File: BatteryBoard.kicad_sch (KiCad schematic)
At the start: 19 parts, among them J1 Keystone-1042, J11 Conn_01x12_MountingPin, J14 Conn_01x04, J15 Conn_01x04, J2 Keystone-1042, J3 Keystone-1042, J4 Keystone-1042, J5 Keystone-1042, J6 Keystone-1042, SW1 SW_SPST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

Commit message: Finish v1 schematic
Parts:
- removed J15: Conn_01x04, symbol Connector_Generic:Conn_01x04
- H1, H2, H3, H4: footprint custom-footprints:MountingHole_3.2mm_M3_DIN965_PadMOD -> BatteryBoard:MountingHole
- J1, J2, J3, J4, J5, J6: footprint KEYSTONE-1042 -> BatteryBoard:Keystone_1042
- J11: value Conn_01x12_MountingPin -> 200528-0120; footprint (none) -> Connector_FFC-FPC:Molex_200528-0120_1x12-1MP_P1.00mm_Horizontal
- J14: value Conn_01x04 -> XT30PW; footprint (none) -> BatteryBoard:AMASS_XT30PW-M; symbol Connector_Generic:Conn_01x04 -> Connector_Generic_MountingPin:Conn_01x02_MountingPin
- SW1, SW2, SW3, SW4: now not fitted
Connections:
- net EN_BURN1 is gone; now on net +3V3: J11.3 (Pin_3)
- net EN_BURN2 is gone; now on net GND: J11.4 (Pin_4)
- net EN_BURN3 is gone; now on net GND: J11.5 (Pin_5)
- net +BATT: no longer J14.1 (Pin_1), J14.2 (Pin_2)
- net B-: now also J5.1 (NEG); no longer J5.2 (POS)
- net BM: now also J5.2 (POS); no longer J5.1 (NEG)
- net GND: now also J14.MP (MountPin); no longer J11.1 (Pin_1), J11.7 (Pin_7), J14.3 (Pin_3), J14.4 (Pin_4)
- net PACK+: now also J14.1 (Pin_1)
- net PACK-: now also J14.2 (Pin_2)
- net BURN_RELAY_A renamed +3V3
- net +3V3: now also J11.1 (Pin_1)
- net EN_BURN4 renamed CHRG_STAT
- net SCL renamed SCL1
- net SDA renamed SDA1
- new net DCHRG_STAT: J11.7 (Pin_7)
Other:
- removed sheet BurnWireControl
- moved on the sheet: H1, H2, H3, H4, J5

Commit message: Cleanup component designators
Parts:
- removed TP19, TP24: TestPoint, TestPoint:TestPoint_Loop_D1.80mm_Drill1.0mm_Beaded, symbol Connector:TestPoint
- added J9: 1985807, symbol Connector_Generic:Conn_01x02
- J8: renamed from J14; value XT30PW -> 1985807; footprint BatteryBoard:AMASS_XT30PW-M -> (none); symbol Connector_Generic_MountingPin:Conn_01x02_MountingPin -> Connector_Generic:Conn_01x02
- renumbered J11 to J7
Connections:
- net GND: no longer J8.MP (MountPin)
- net PACK+: now also J9.1 (Pin_1)
- net PACK-: now also J9.2 (Pin_2)
- net Fuel_Alert renamed ALRT
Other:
- note added: "FPC Ribbon cable I/O Connection to Mainboard"
- note added: "Terminal Block Power Connection to Mainboard"
- note removed: "FPC Ribbon cable I/O Connections to Mainboard"
- moved on the sheet: J7

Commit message: Complete layout
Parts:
- removed J1, J2, J3, J4: Keystone-1042, BatteryBoard:Keystone_1042, symbol BatteryBoard:Keystone-1042
- removed J8, J9: 1985807, symbol Connector_Generic:Conn_01x02
- removed SW1, SW2, SW3, SW4: SW_SPST, symbol Switch:SW_SPST
- added J1, J3: Keystone-1048, BatteryBoard:BAT_1048, symbol BatteryBoard:Keystone-1048
- added J8: 282834-4, BatteryBoard:TE_282834-4, symbol Connector_Generic:Conn_01x04
- J7: value 200528-0120 -> 200528-0100; footprint Connector_FFC-FPC:Molex_200528-0120_1x12-1MP_P1.00mm_Horizontal -> Connector_FFC-FPC:Molex_200528-0100_1x10-1MP_P1.00mm_Horizontal; symbol Connector_Generic_MountingPin:Conn_01x12_MountingPin -> Connector_Generic_MountingPin:Conn_01x10_MountingPin
- renumbered J5 to J2, J6 to J4
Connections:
- net CHRG_STAT is gone; now on net SDA1: J7.6 (Pin_6)
- net DCHRG_STAT is gone; now on net GND: J7.7 (Pin_7)
- net +3V3: now also J7.10 (Pin_10), J7.9 (Pin_9); no longer J7.1 (Pin_1), J7.2 (Pin_2), J7.3 (Pin_3)
- net ALRT: now also J7.4 (Pin_4); no longer J7.10 (Pin_10)
- net B+: now also J3.2 (POS), J3.4 (POS)
- net B-: now also J1.1 (NEG), J1.3 (NEG)
- net BM: now also J1.2 (POS), J1.4 (POS), J3.1 (NEG), J3.3 (NEG)
- net GND: now also J7.1 (Pin_1), J7.8 (Pin_8); no longer J7.11 (Pin_11), J7.12 (Pin_12), J7.4 (Pin_4), J7.5 (Pin_5)
- net PACK+: now also J8.1 (Pin_1), J8.3 (Pin_3)
- net PACK-: now also J8.2 (Pin_2), J8.4 (Pin_4)
- net SCL1: now also J7.5 (Pin_5); no longer J7.8 (Pin_8)
- net SDA1: no longer J7.9 (Pin_9)
- new net CSTAT: J7.3 (Pin_3)
- new net DSTAT: J7.2 (Pin_2)
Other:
- note removed: "INHIBIT SWITCHES"
- note removed: "Normally closed inhibit switches Disconnect PACK+ from +BATT when pressed (High-side inhibit) Disconnect PACK- from GND when pressed (Low-side inhibit)"
- moved on the sheet: H1, H2, H3, H4, J2, J4

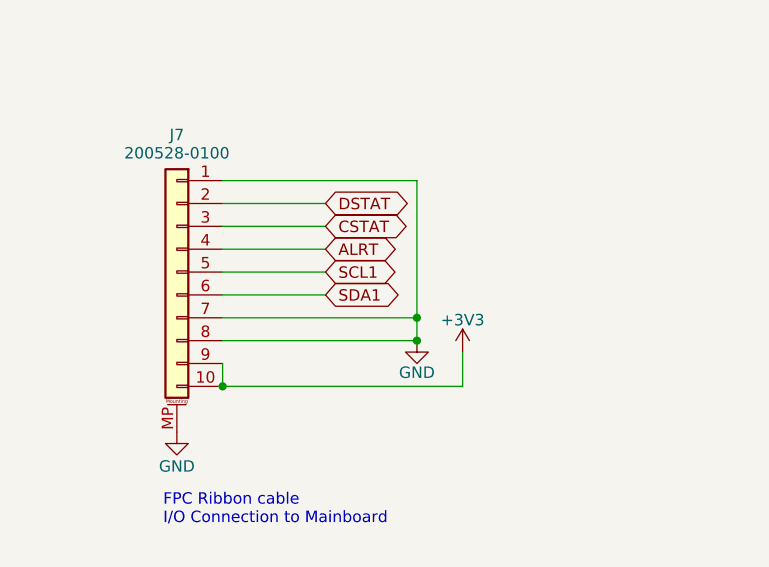
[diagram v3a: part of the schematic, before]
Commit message: Relabeled I2C nets for accuracy
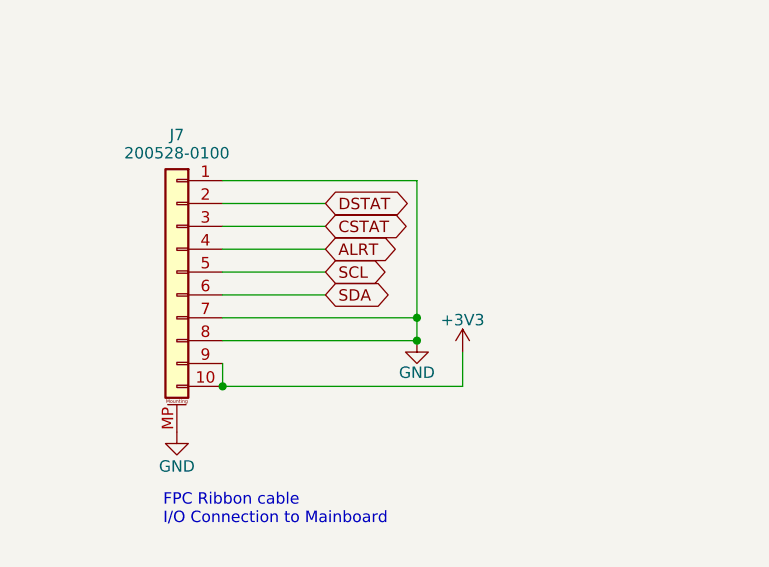
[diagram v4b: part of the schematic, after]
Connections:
- net SCL1 renamed SCL
- net SDA1 renamed SDA
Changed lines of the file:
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@@
 		)
 	)
-	(global_label "SDA1"
+	(global_label "SDA"
 		(shape bidirectional)
 		(at 90.17 137.16 0)
@@
 		)
 		(property "Intersheetrefs" "${INTERSHEET_REFS}"
-			(at 98.2311 137.16 0)
+			(at 97.0216 137.16 0)
 			(effects
 				(font
@@
 		)
 	)
-	(global_label "SCL1"
+	(global_label "SCL"
 		(shape bidirectional)
 		(at 90.17 134.62 0)
@@
 		)
 		(property "Intersheetrefs" "${INTERSHEET_REFS}"
-			(at 98.1706 134.62 0)
+			(at 96.9611 134.62 0)
 			(effects
 				(font
